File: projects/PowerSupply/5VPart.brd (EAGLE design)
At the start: 50 x 50 mm, 26 parts, among them IC1 LM2596T, IC2 LM2596T, X1 IN, X2 OUT

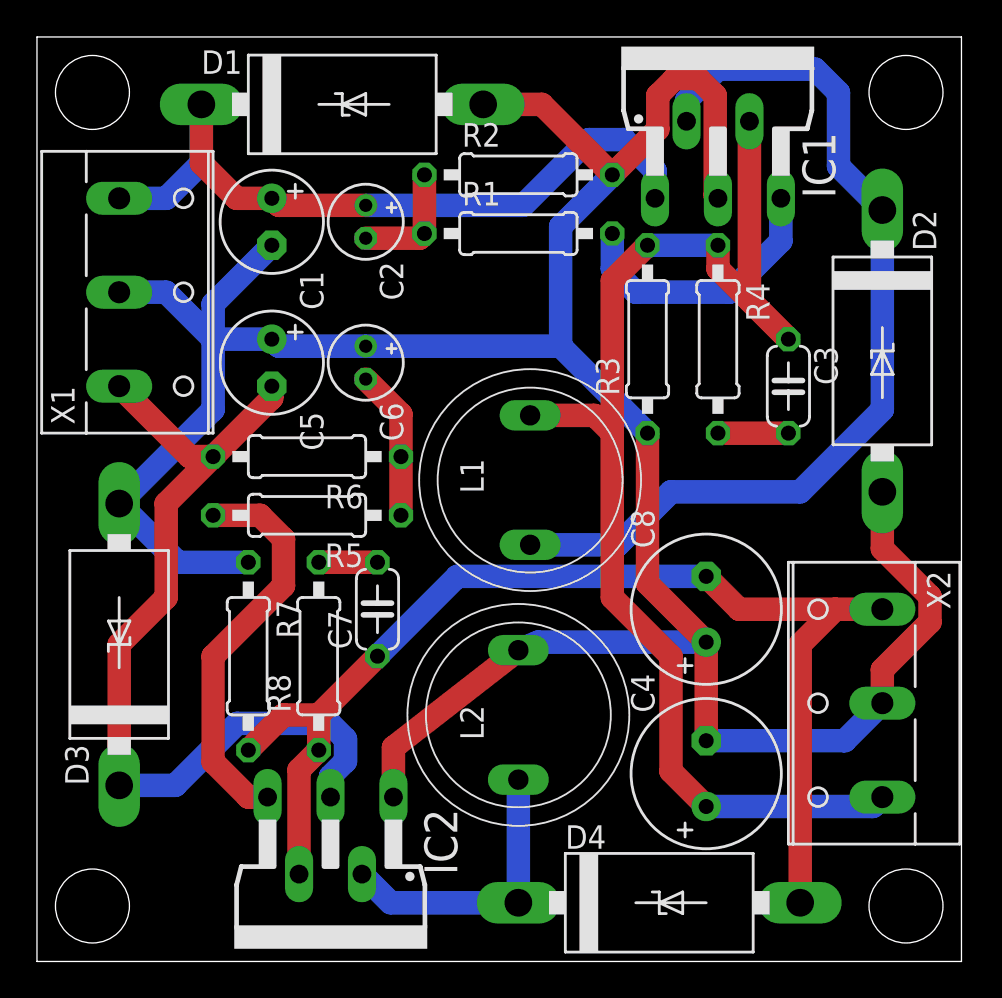
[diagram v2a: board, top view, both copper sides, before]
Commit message: feat: 5 volt part rerouted
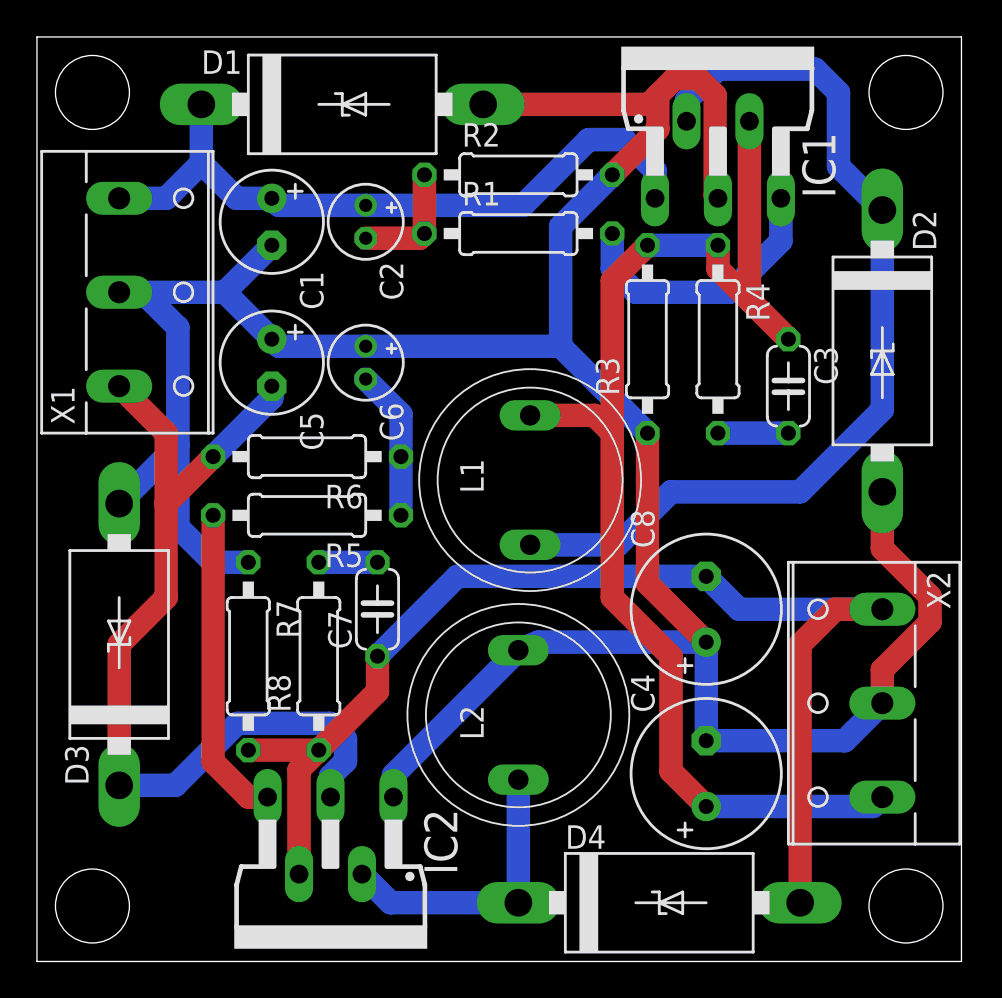
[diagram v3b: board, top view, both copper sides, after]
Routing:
- net N$7: track 21.7 -> 17.1 mm
- net +20V: track 40.7 -> 37.6 mm
- net GND: track 154.6 -> 156.9 mm
- net -5V: track 64.6 -> 66.4 mm
- net -20V: track 49.1 -> 49.9 mm
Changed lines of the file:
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@@
 <contactref element="X2" pad="2"/>
 <contactref element="X1" pad="2"/>
-<wire x1="19.2786" y1="8.89" x2="19.2786" y2="11.5786" width="1.27" layer="1"/>
-<wire x1="19.2786" y1="11.5786" x2="26.035" y2="16.835" width="1.27" layer="1"/>
-<wire x1="36.195" y1="11.938" x2="36.195" y2="17.272" width="1.27" layer="1"/>
 <wire x1="36.195" y1="17.272" x2="33.02" y2="20.447" width="1.27" layer="1"/>
 <wire x1="33.02" y1="20.447" x2="33.02" y2="28.575" width="1.27" layer="1"/>
@@
 <wire x1="36.83" y1="41.275" x2="36.6776" y2="41.4274" width="1.27" layer="1"/>
 <wire x1="36.6776" y1="41.4274" x2="36.6776" y2="46.8443875" width="1.27" layer="1"/>
-<wire x1="24.13" y1="46.355" x2="27.305" y2="46.355" width="1.27" layer="1"/>
-<wire x1="27.305" y1="46.355" x2="31.115" y2="42.545" width="1.27" layer="1"/>
 <wire x1="48.2981" y1="18.35298125" x2="48.2981" y2="19.74701875" width="1.27" layer="1"/>
 <wire x1="45.72" y1="22.32511875" x2="45.72" y2="25.4" width="1.27" layer="1"/>
@@
 <wire x1="31.115" y1="42.545" x2="28.321" y2="39.751" width="1.27" layer="16"/>
 <wire x1="28.321" y1="39.751" x2="28.321" y2="33.274" width="1.27" layer="16"/>
-<wire x1="11.43" y1="21.59" x2="7.62" y2="21.59" width="1.27" layer="16"/>
-<wire x1="7.62" y1="21.59" x2="4.445" y2="24.765" width="1.27" layer="16"/>
-<wire x1="4.445" y1="24.765" x2="9.525" y2="29.845" width="1.27" layer="16"/>
-<wire x1="9.525" y1="29.845" x2="9.525" y2="33.655" width="1.27" layer="16"/>
-<wire x1="9.525" y1="33.655" x2="6.985" y2="36.195" width="1.27" layer="16"/>
-<wire x1="6.985" y1="36.195" x2="4.445" y2="36.195" width="1.27" layer="16"/>
-<wire x1="12.7" y1="33.655" x2="9.525" y2="33.655" width="1.27" layer="16"/>
-<wire x1="12.7" y1="38.735" x2="9.525" y2="35.56" width="1.27" layer="16"/>
-<wire x1="9.525" y1="35.56" x2="9.525" y2="33.655" width="1.27" layer="16"/>
+<wire x1="36.195" y1="11.938" x2="36.195" y2="17.272" width="1.27" layer="16"/>
+<wire x1="19.2786" y1="8.89" x2="19.2786" y2="10.0786" width="1.27" layer="16"/>
+<wire x1="19.2786" y1="10.0786" x2="26.035" y2="16.835" width="1.27" layer="16"/>
 <wire x1="17.78" y1="33.274" x2="13.081" y2="33.274" width="1.27" layer="16"/>
 <wire x1="13.081" y1="33.274" x2="12.7" y2="33.655" width="1.27" layer="16"/>
+<wire x1="10.16" y1="36.195" x2="12.7" y2="33.655" width="1.27" layer="16"/>
+<wire x1="4.445" y1="36.195" x2="10.16" y2="36.195" width="1.27" layer="16"/>
+<wire x1="10.16" y1="36.195" x2="12.7" y2="38.735" width="1.27" layer="16"/>
+<wire x1="11.43" y1="21.59" x2="9.525" y2="21.59" width="1.27" layer="16"/>
+<wire x1="9.525" y1="21.59" x2="7.62" y2="23.495" width="1.27" layer="16"/>
+<wire x1="7.62" y1="23.495" x2="7.62" y2="27.94" width="1.27" layer="16"/>
+<wire x1="7.62" y1="27.94" x2="7.62" y2="34.29" width="1.27" layer="16"/>
+<wire x1="7.62" y1="34.29" x2="5.715" y2="36.195" width="1.27" layer="16"/>
+<wire x1="5.715" y1="36.195" x2="4.445" y2="36.195" width="1.27" layer="16"/>
+<wire x1="4.445" y1="24.765" x2="7.62" y2="27.94" width="1.27" layer="16"/>
+<wire x1="33.0894125" y1="46.355" x2="33.5788" y2="46.8443875" width="1.27" layer="1"/>
+<wire x1="24.13" y1="46.355" x2="33.0894125" y2="46.355" width="1.27" layer="1"/>
 </signal>
 <signal name="N$3">
@@
 <contactref element="R8" pad="2"/>
 <contactref element="C7" pad="2"/>
-<wire x1="18.415" y1="21.59" x2="15.24" y2="21.59" width="1.27" layer="1"/>
+<wire x1="15.24" y1="21.59" x2="18.415" y2="21.59" width="1.27" layer="16"/>
 </signal>
 <signal name="N$1">
 <contactref element="R4" pad="2"/>
 <contactref element="C3" pad="2"/>
-<wire x1="36.83" y1="28.575" x2="40.64" y2="28.575" width="1.27" layer="1"/>
+<wire x1="36.83" y1="28.575" x2="40.64" y2="28.575" width="1.27" layer="16"/>
 </signal>
 <signal name="N$4">
@@
 <contactref element="R5" pad="2"/>
 <contactref element="IC2" pad="5"/>
-<wire x1="9.525" y1="24.13" x2="12.065" y2="24.13" width="1.27" layer="1"/>
-<wire x1="12.065" y1="24.13" x2="13.335" y2="22.86" width="1.27" layer="1"/>
-<wire x1="13.335" y1="22.86" x2="13.335" y2="20.32" width="1.27" layer="1"/>
-<wire x1="13.335" y1="20.32" x2="9.525" y2="16.51" width="1.27" layer="1"/>
-<wire x1="9.525" y1="16.51" x2="9.525" y2="10.795" width="1.27" layer="1"/>
-<wire x1="9.525" y1="10.795" x2="11.43" y2="8.89" width="1.27" layer="1"/>
+<wire x1="11.43" y1="8.89" x2="9.525" y2="10.795" width="1.27" layer="1"/>
 <wire x1="11.43" y1="8.89" x2="12.4714" y2="8.89" width="1.27" layer="1"/>
+<wire x1="9.525" y1="10.795" x2="9.525" y2="24.13" width="1.27" layer="1"/>
 </signal>
 <signal name="N$8">
@@
 <contactref element="C6" pad="-"/>
 <contactref element="R6" pad="1"/>
-<wire x1="19.685" y1="24.13" x2="19.685" y2="27.305" width="1.27" layer="1"/>
-<wire x1="17.78" y1="31.496" x2="19.685" y2="29.591" width="1.27" layer="1"/>
-<wire x1="19.685" y1="29.591" x2="19.685" y2="27.305" width="1.27" layer="1"/>
+<wire x1="17.78" y1="31.496" x2="19.685" y2="29.591" width="1.27" layer="16"/>
+<wire x1="19.685" y1="29.591" x2="19.685" y2="27.305" width="1.27" layer="16"/>
+<wire x1="19.685" y1="27.305" x2="19.685" y2="24.13" width="1.27" layer="16"/>
 </signal>
 <signal name="+5V">
@@
 <contactref element="C7" pad="1"/>
 <contactref element="D4" pad="A"/>
+<contactref element="X2" pad="3"/>
+<wire x1="43.18" y1="19.05" x2="45.72" y2="19.05" width="1.27" layer="1"/>
+<wire x1="41.275" y1="17.145" x2="43.18" y2="19.05" width="1.27" layer="1"/>
+<wire x1="41.275" y1="3.175" x2="41.275" y2="17.145" width="1.27" layer="1"/>
+<wire x1="18.415" y1="16.51" x2="22.733" y2="20.828" width="1.27" layer="16"/>
+<wire x1="22.733" y1="20.828" x2="36.195" y2="20.828" width="1.27" layer="16"/>
+<wire x1="45.72" y1="19.05" x2="37.973" y2="19.05" width="1.27" layer="16"/>
+<wire x1="37.973" y1="19.05" x2="36.195" y2="20.828" width="1.27" layer="16"/>
+<wire x1="11.43" y1="11.43" x2="15.24" y2="11.43" width="1.27" layer="1"/>
 <wire x1="14.1732" y1="4.7244" x2="14.1732" y2="10.3632" width="1.27" layer="1"/>
 <wire x1="14.1732" y1="10.3632" x2="15.24" y2="11.43" width="1.27" layer="1"/>
-<wire x1="15.24" y1="11.43" x2="15.24" y2="13.335" width="1.27" layer="1"/>
-<wire x1="15.24" y1="13.335" x2="18.415" y2="16.51" width="1.27" layer="1"/>
-<contactref element="X2" pad="3"/>
-<wire x1="37.973" y1="19.05" x2="43.18" y2="19.05" width="1.27" layer="1"/>
-<wire x1="43.18" y1="19.05" x2="45.72" y2="19.05" width="1.27" layer="1"/>
-<wire x1="41.275" y1="17.145" x2="43.18" y2="19.05" width="1.27" layer="1"/>
-<wire x1="36.195" y1="20.828" x2="37.973" y2="19.05" width="1.27" layer="1"/>
-<wire x1="41.275" y1="3.175" x2="41.275" y2="17.145" width="1.27" layer="1"/>
-<wire x1="11.43" y1="11.43" x2="13.335" y2="13.335" width="1.27" layer="1"/>
-<wire x1="13.335" y1="13.335" x2="15.24" y2="13.335" width="1.27" layer="1"/>
-<wire x1="18.415" y1="16.51" x2="22.733" y2="20.828" width="1.27" layer="16"/>
-<wire x1="22.733" y1="20.828" x2="36.195" y2="20.828" width="1.27" layer="16"/>
+<wire x1="18.415" y1="14.605" x2="18.415" y2="16.51" width="1.27" layer="1"/>
+<wire x1="18.415" y1="14.605" x2="15.24" y2="11.43" width="1.27" layer="1"/>
 </signal>
 <signal name="+20V">
@@
 <contactref element="C2" pad="+"/>
 <contactref element="D1" pad="C"/>
-<wire x1="10.795" y1="41.275" x2="8.89" y2="43.18" width="1.27" layer="1"/>
-<wire x1="10.795" y1="41.275" x2="12.7" y2="41.275" width="1.27" layer="1"/>
-<wire x1="17.78" y1="40.894" x2="13.081" y2="40.894" width="1.27" layer="1"/>
-<wire x1="13.081" y1="40.894" x2="12.7" y2="41.275" width="1.27" layer="1"/>
 <wire x1="17.78" y1="40.894" x2="26.289" y2="40.894" width="1.27" layer="16"/>
 <wire x1="26.289" y1="40.894" x2="29.845" y2="44.45" width="1.27" layer="16"/>
@@
 <wire x1="8.89" y1="43.18" x2="6.985" y2="41.275" width="1.27" layer="16"/>
 <wire x1="6.985" y1="41.275" x2="4.445" y2="41.275" width="1.27" layer="16"/>
-<wire x1="8.89" y1="43.18" x2="8.89" y2="46.355" width="1.27" layer="1"/>
+<wire x1="12.7" y1="41.275" x2="10.795" y2="41.275" width="1.27" layer="16"/>
+<wire x1="10.795" y1="41.275" x2="8.89" y2="43.18" width="1.27" layer="16"/>
+<wire x1="17.78" y1="40.894" x2="13.081" y2="40.894" width="1.27" layer="16"/>
+<wire x1="13.081" y1="40.894" x2="12.7" y2="41.275" width="1.27" layer="16"/>
 </signal>
 <signal name="-20V">
@@
 <wire x1="6.985" y1="19.685" x2="6.985" y2="24.765" width="1.27" layer="1"/>
 <wire x1="6.985" y1="24.765" x2="9.525" y2="27.305" width="1.27" layer="1"/>
-<wire x1="9.525" y1="27.305" x2="12.7" y2="30.48" width="1.27" layer="1"/>
-<wire x1="12.7" y1="30.48" x2="12.7" y2="31.115" width="1.27" layer="1"/>
-<wire x1="9.525" y1="27.305" x2="8.255" y2="27.305" width="1.27" layer="1"/>
-<wire x1="8.255" y1="27.305" x2="4.445" y2="31.115" width="1.27" layer="1"/>
+<wire x1="9.525" y1="27.305" x2="12.7" y2="30.48" width="1.27" layer="16"/>
+<wire x1="12.7" y1="30.48" x2="12.7" y2="31.115" width="1.27" layer="16"/>
+<wire x1="4.445" y1="31.115" x2="6.985" y2="28.575" width="1.27" layer="1"/>
+<wire x1="6.985" y1="28.575" x2="6.985" y2="24.765" width="1.27" layer="1"/>
 </signal>
 </signals>

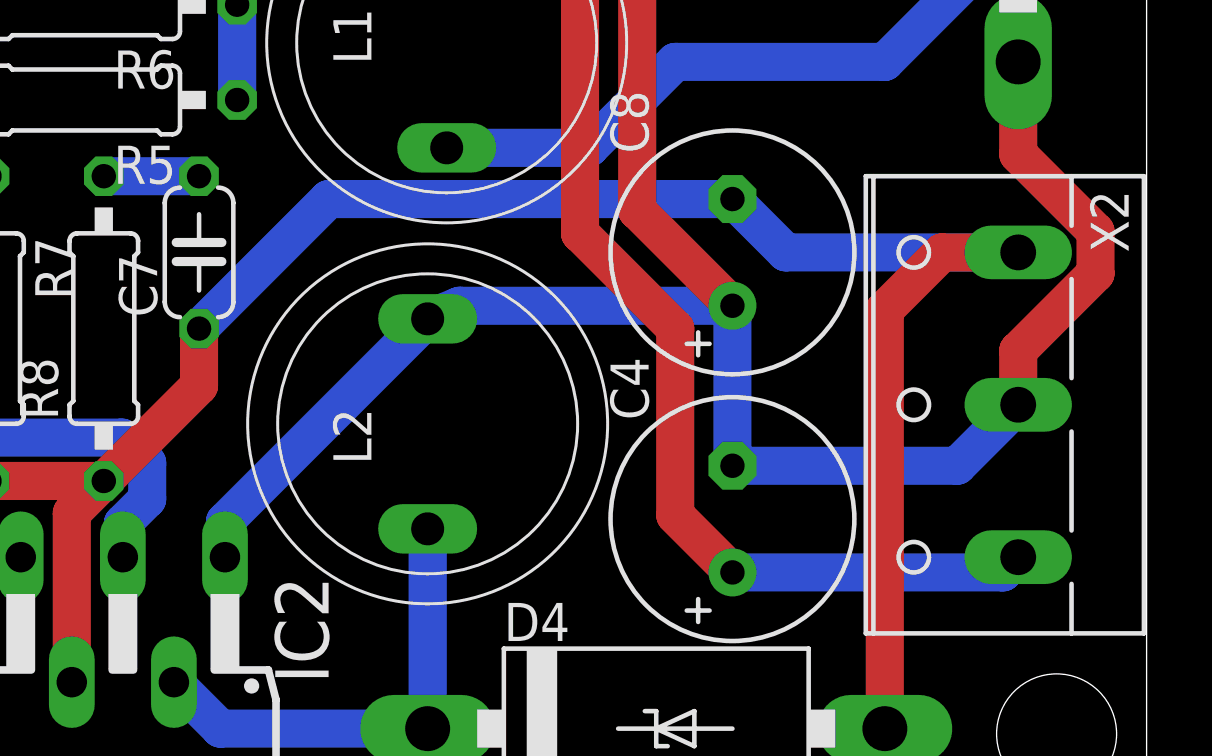
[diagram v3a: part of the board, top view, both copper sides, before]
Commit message: feat: 5 volt part rerouted
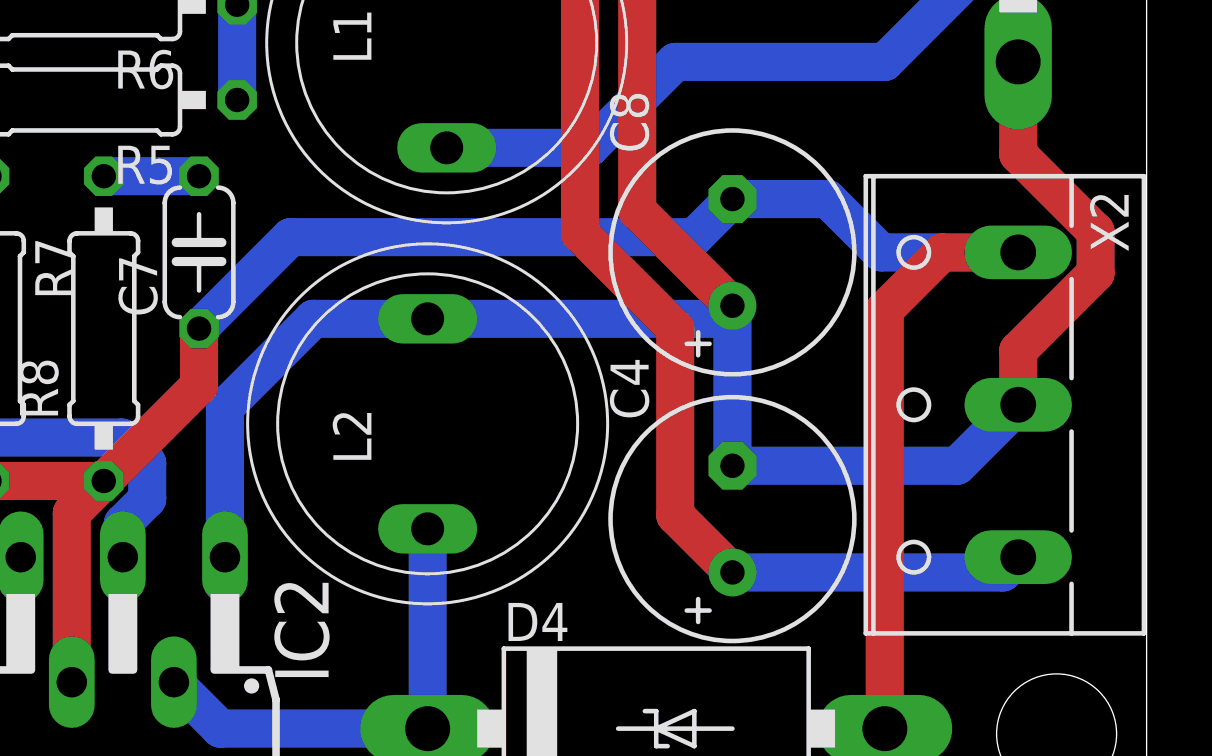
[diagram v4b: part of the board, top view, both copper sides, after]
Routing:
- net GND: track 156.9 -> 159.3 mm
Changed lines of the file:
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@@
 <wire x1="36.195" y1="11.938" x2="43.688" y2="11.938" width="1.27" layer="16"/>
 <wire x1="43.688" y1="11.938" x2="45.72" y2="13.97" width="1.27" layer="16"/>
-<wire x1="36.195" y1="17.272" x2="27.098" y2="17.272" width="1.27" layer="16"/>
-<wire x1="27.098" y1="17.272" x2="26.035" y2="16.835" width="1.27" layer="16"/>
 <wire x1="17.78" y1="33.274" x2="28.321" y2="33.274" width="1.27" layer="16"/>
 <wire x1="28.321" y1="33.274" x2="33.02" y2="28.575" width="1.27" layer="16"/>
@@
 <wire x1="28.321" y1="39.751" x2="28.321" y2="33.274" width="1.27" layer="16"/>
 <wire x1="36.195" y1="11.938" x2="36.195" y2="17.272" width="1.27" layer="16"/>
-<wire x1="19.2786" y1="8.89" x2="19.2786" y2="10.0786" width="1.27" layer="16"/>
-<wire x1="19.2786" y1="10.0786" x2="26.035" y2="16.835" width="1.27" layer="16"/>
+<wire x1="19.2786" y1="8.89" x2="19.2786" y2="13.8886" width="1.27" layer="16"/>
+<wire x1="22.225" y1="16.835" x2="26.035" y2="16.835" width="1.27" layer="16"/>
+<wire x1="22.225" y1="16.835" x2="19.2786" y2="13.8886" width="1.27" layer="16"/>
 <wire x1="17.78" y1="33.274" x2="13.081" y2="33.274" width="1.27" layer="16"/>
 <wire x1="13.081" y1="33.274" x2="12.7" y2="33.655" width="1.27" layer="16"/>
@@
 <wire x1="33.0894125" y1="46.355" x2="33.5788" y2="46.8443875" width="1.27" layer="1"/>
 <wire x1="24.13" y1="46.355" x2="33.0894125" y2="46.355" width="1.27" layer="1"/>
+<wire x1="26.035" y1="16.835" x2="35.758" y2="16.835" width="1.27" layer="16"/>
+<wire x1="35.758" y1="16.835" x2="36.195" y2="17.272" width="1.27" layer="16"/>
 </signal>
 <signal name="N$3">
@@
 <wire x1="41.275" y1="17.145" x2="43.18" y2="19.05" width="1.27" layer="1"/>
 <wire x1="41.275" y1="3.175" x2="41.275" y2="17.145" width="1.27" layer="1"/>
-<wire x1="18.415" y1="16.51" x2="22.733" y2="20.828" width="1.27" layer="16"/>
-<wire x1="22.733" y1="20.828" x2="36.195" y2="20.828" width="1.27" layer="16"/>
-<wire x1="45.72" y1="19.05" x2="37.973" y2="19.05" width="1.27" layer="16"/>
-<wire x1="37.973" y1="19.05" x2="36.195" y2="20.828" width="1.27" layer="16"/>
+<wire x1="18.415" y1="16.51" x2="21.463" y2="19.558" width="1.27" layer="16"/>
+<wire x1="34.925" y1="19.558" x2="36.195" y2="20.828" width="1.27" layer="16"/>
+<wire x1="34.925" y1="19.558" x2="21.463" y2="19.558" width="1.27" layer="16"/>
+<wire x1="45.72" y1="19.05" x2="41.148" y2="19.05" width="1.27" layer="16"/>
+<wire x1="41.148" y1="19.05" x2="39.37" y2="20.828" width="1.27" layer="16"/>
+<wire x1="39.37" y1="20.828" x2="36.195" y2="20.828" width="1.27" layer="16"/>
 <wire x1="11.43" y1="11.43" x2="15.24" y2="11.43" width="1.27" layer="1"/>
 <wire x1="14.1732" y1="4.7244" x2="14.1732" y2="10.3632" width="1.27" layer="1"/>
